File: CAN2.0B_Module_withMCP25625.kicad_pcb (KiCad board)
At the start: 2 copper layers, 27.9 x 25.4 mm, 16 parts, among them J1 Conn_01x05_Pin, J2 Conn_01x05_Pin, SW1 SW_DPDT_x2, SW2 SW_Push, U1 LM1117MP-3.3, U3 MCP25625-x-SS

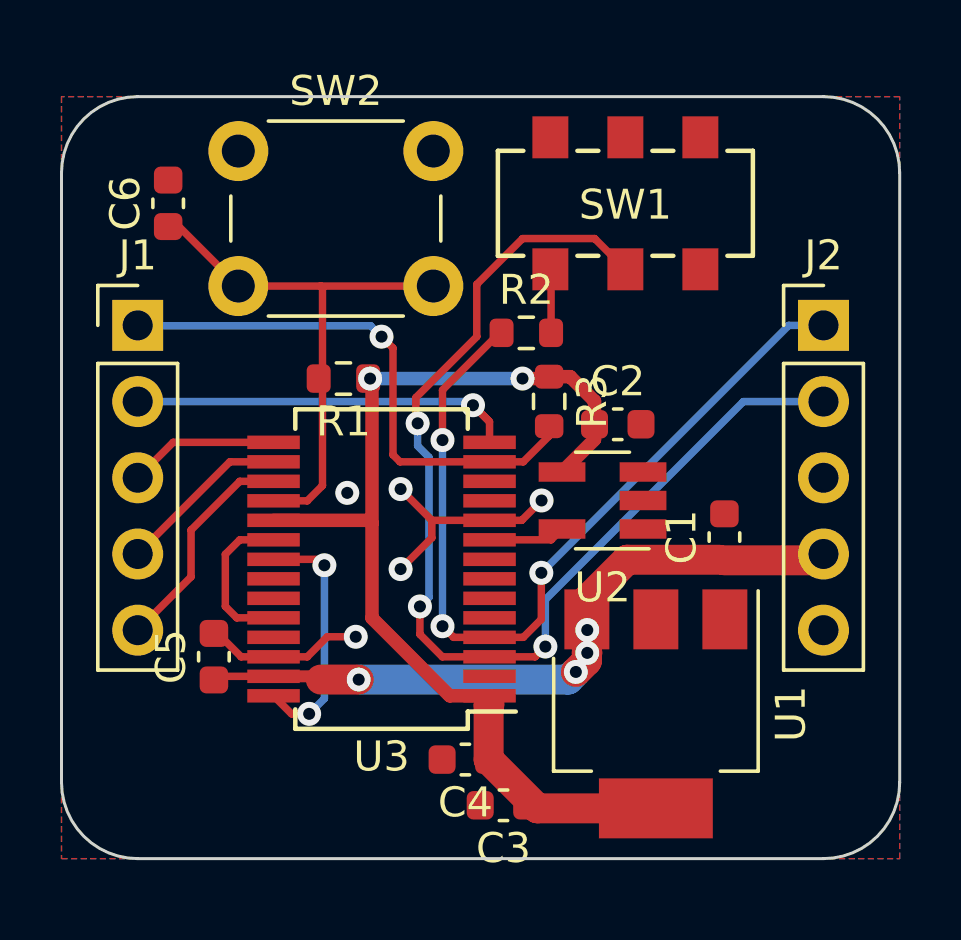
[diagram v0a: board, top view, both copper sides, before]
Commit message: add via
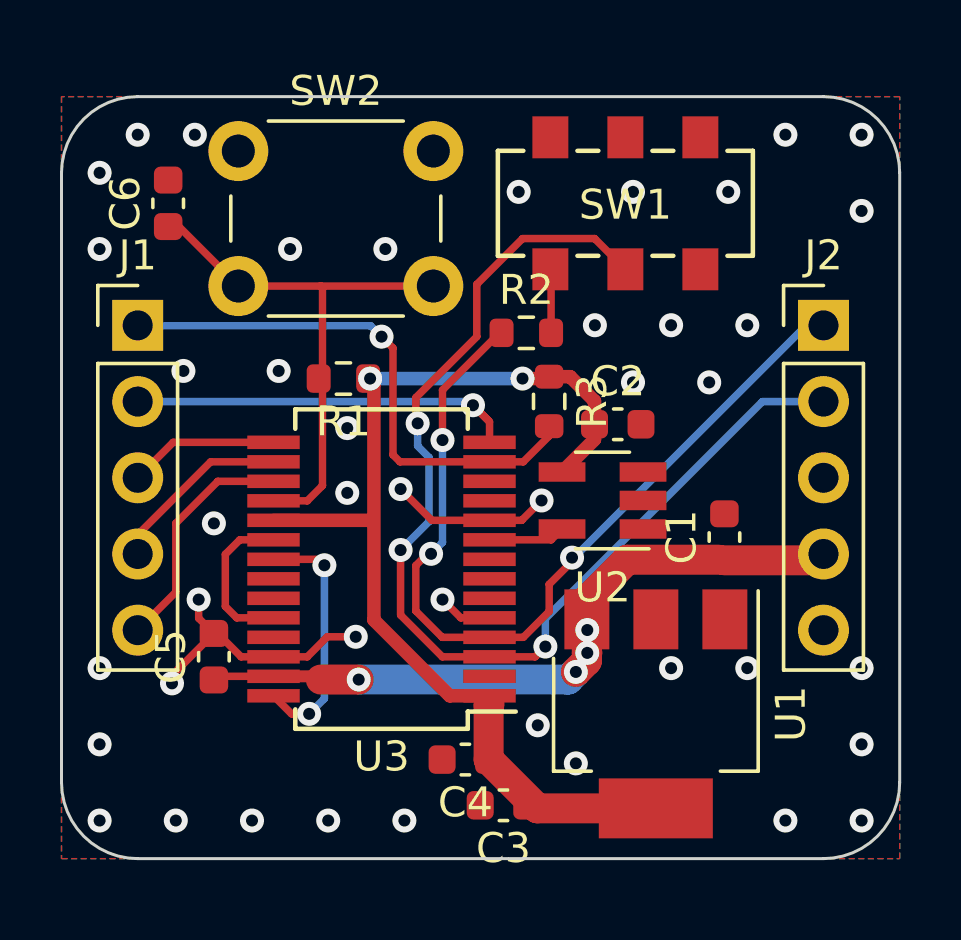
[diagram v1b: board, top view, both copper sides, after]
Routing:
- net GND: track 12.8 -> 16.2 mm, vias 5 -> 43
- net CANH: track 28.7 -> 29.4 mm
